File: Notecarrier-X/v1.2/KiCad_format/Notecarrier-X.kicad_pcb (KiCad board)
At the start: 2 copper layers, 66.1 x 38.1 mm, 56 parts, among them J1 SM04B-SRSS-TB(LF)(SN), J2 S2B-PH-SM4-K-TB, J3 MDT420E01001, J4 SF72S006VBDR2500, P1 Header 2.54mm 1x16, P2 Header 2.54mm 1x16, P3 SM05B-SRSS-TB, P4 12402012E212A, U1 ISL9122AIINZ-T, U2 BQ25628ERYKR, U3 LM66200DRLR

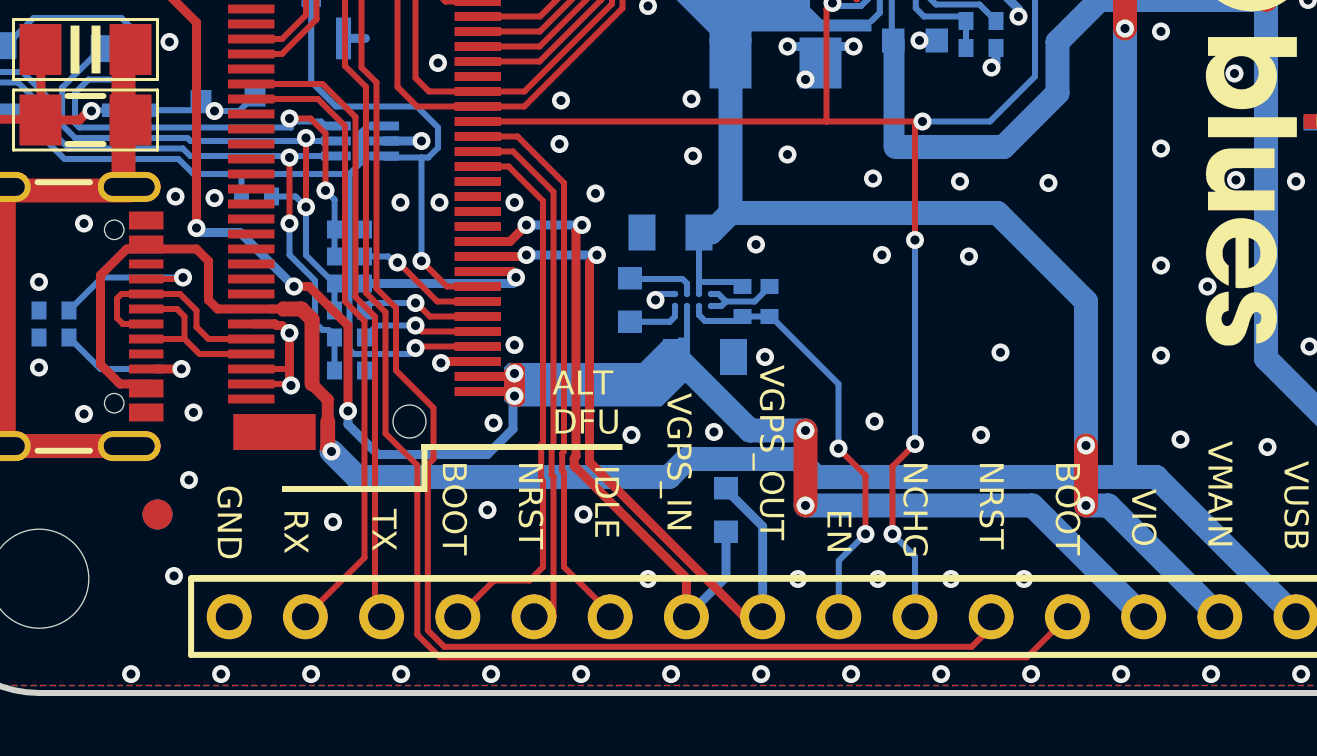
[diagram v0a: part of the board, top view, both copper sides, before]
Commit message: feat: updates to X, XM, XS Notecarrier files (#49)
* Notecarrier-X/XM: add board-regeneration scripts

Scripts used to regenerate the X and XM v1.2 boards from the design
house's Rev-11 release snapshots while keeping everything else in the
published ports:

- sanitize_fonts.py: zero the padding after each Texts6 font name in a
  copy of the PcbDoc. KiCad 9.0.9's Altium importer converts the whole
  64-byte UTF-16 field, and leftover bytes containing an unpaired
  surrogate make it drop the TrueType face (and size the text as
  stroke text).
- pcb_import.py: headless PcbDoc -> .kicad_pcb import.
- transplant.py: swap the Rev-11 tracks, vias, zones (original fills)
  and board graphics into the published port's file, renumbering nets
  by name through pad correspondence; 3-way merge for the moved jumper.

Co-Authored-By: Claude Opus 5.5 <noreply@anthropic.com>

* Notecarrier-X v1.2: regenerate board from the Rev-11 release snapshot

The port was first built from a post-v1.2 development state and carried
a source-fidelity disclaimer (silk read V1.3; the production-DNP jumper
R4 sat on the bottom side). The design house has now supplied the Rev-11
snapshot behind the published v1.2 fab package (2200-918, 3000-794-001).

- Schematic unchanged: the Rev-11 electrical sheets are identical in
  substance to the development state (template differences only).
- Board regenerated from Rev-11: R4 back on top with its local routing,
  re-poured GND fills, silk V1.2 / RST. Footprints, schematic links,
  BOM fields, rules and project settings carried over unchanged.
- Verified: all harness gates pass; copper/mask/paste 0.001-0.010 vs the
  published fab with no difference cluster >= 0.045 mm2 (baseline
  tightened); every pad's net matches the Rev-11 board
  (validation/altium-netlist-compare.txt, 0 conflicts, 56 nets).
- Fab zip and layer PDF re-exported; Porting-Notes and READMEs updated,
  disclaimer retired.

Co-Authored-By: Claude Opus 5.5 <noreply@anthropic.com>

* Notecarri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
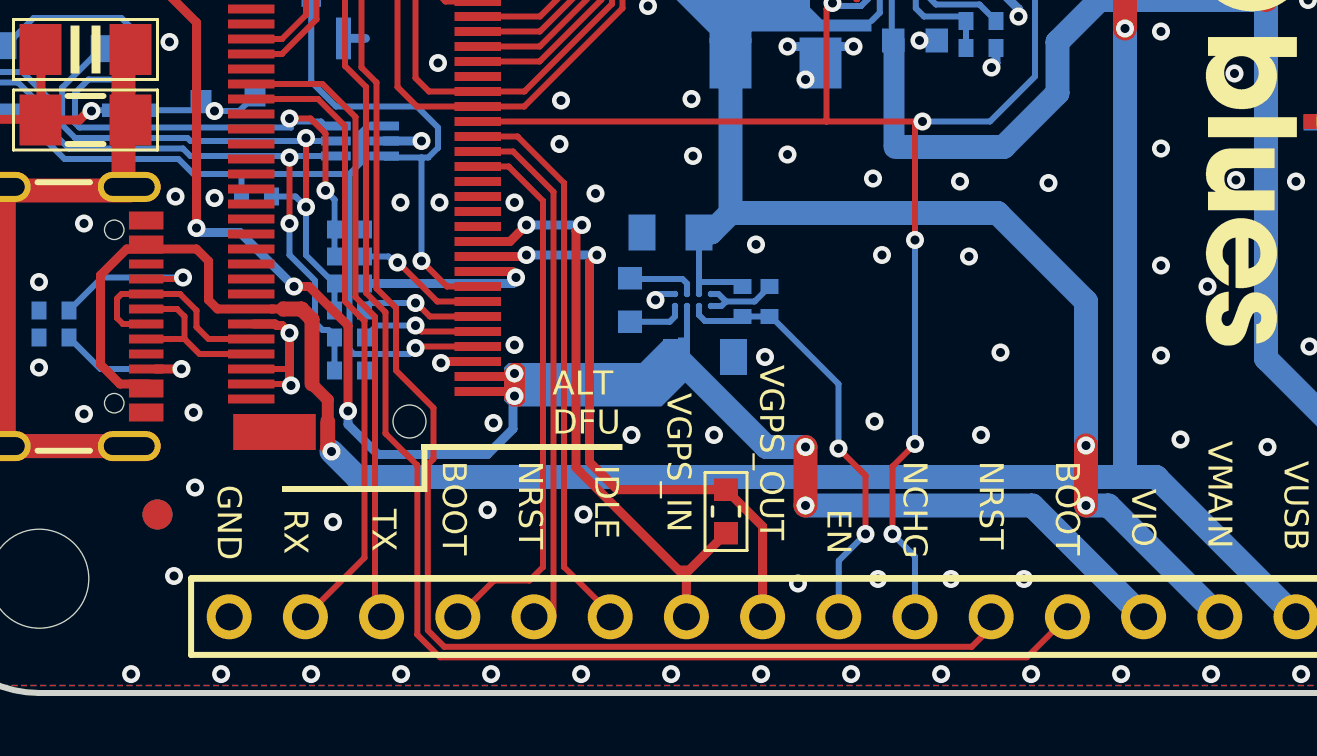
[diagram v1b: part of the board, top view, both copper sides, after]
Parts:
- R4: moved to F.Cu
- moved R4 0.05 mm to (142.1, 118.0)
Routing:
- net +VACT_GPS_OUT: track 24.6 -> 20.7 mm
- net +VACT_GPS_IN: track 21.8 -> 20.4 mm
- net GND: vias 146 -> 145
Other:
- board text added: "217"
- board text added: "262 Total"
- board text added: "RST"
- board text removed: "218"
- board text removed: "263 Total"
